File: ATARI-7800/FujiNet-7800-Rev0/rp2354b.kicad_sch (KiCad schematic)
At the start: 46 parts, among them J2 DBG UART, Q1 2N7002, SW1 RESET, SW2 BOOTSEL, U1 RP2354B, Y1 12MHz

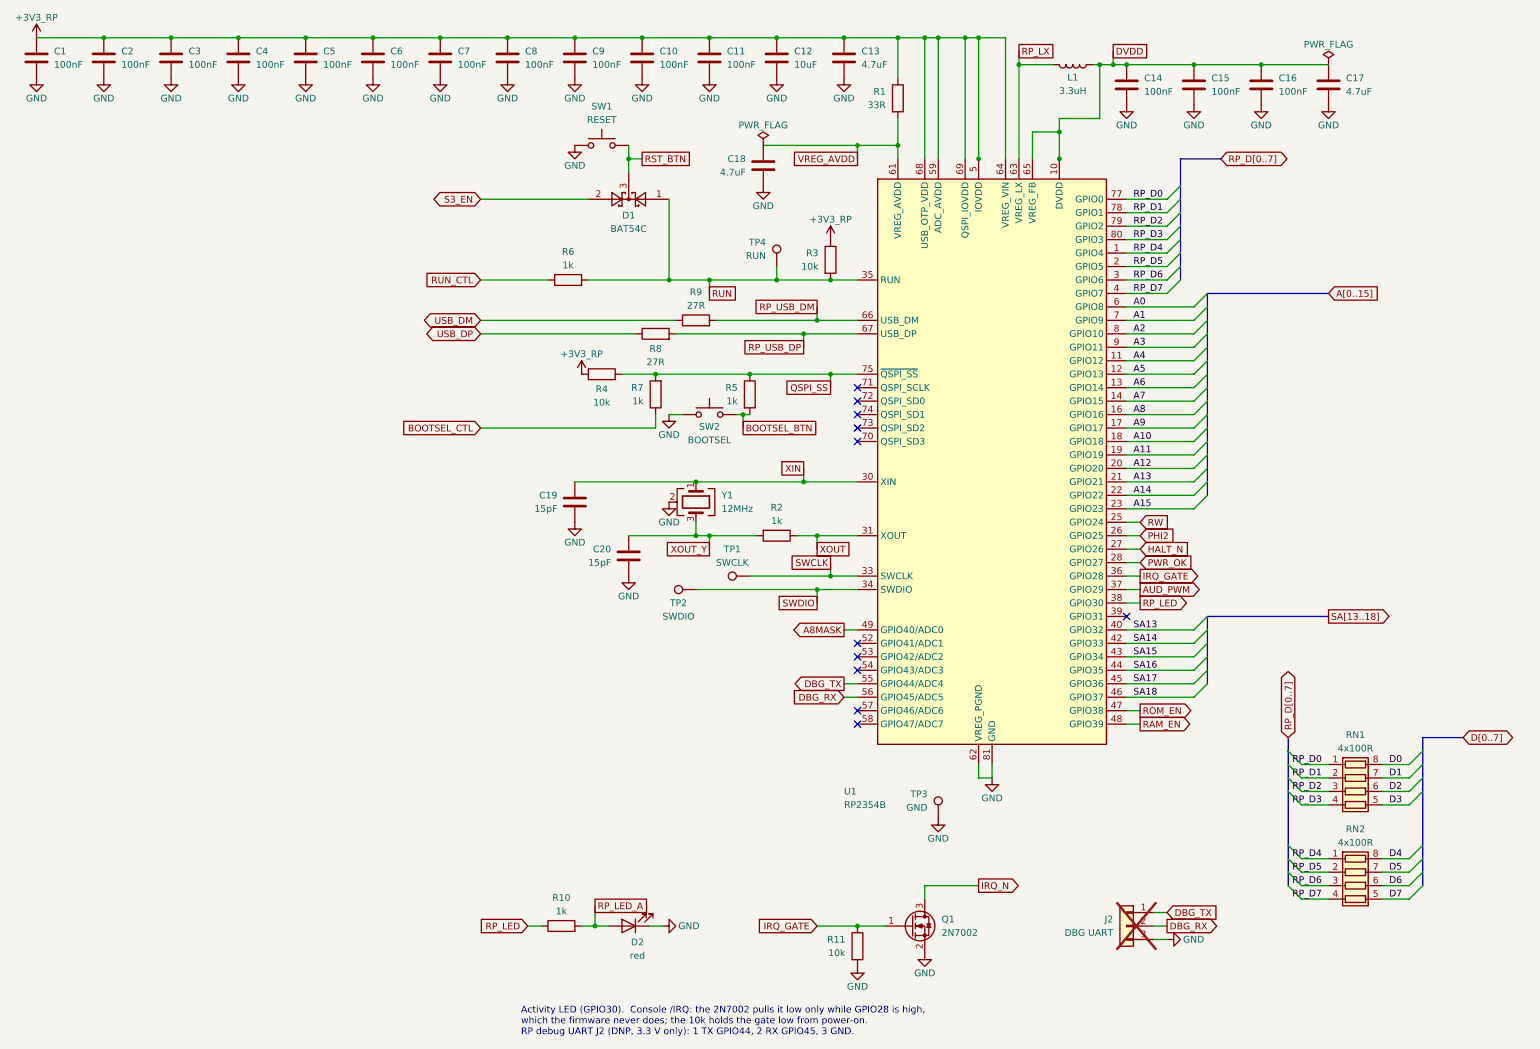
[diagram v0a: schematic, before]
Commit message: ATARI-7800 Rev0: fix the edge, audit the circuit, redraw from the slot, place the board
Edge (board-killer in the schematic-only footprint): the 7800 edge has 18
positions at 2.54 mm with key slots at 3 and 16 for the console's plastic
keys. Pins 1, 2, 15, 16 (and 32, 31, 18, 17) sat one pitch inward, on the
key positions, with no slots and a 42.6 mm tab. tools/edge_geom.py now holds
the geometry (47.0 mm tab, slots centred on +-16.51, 2.4 x 10 mm);
tools/audit/edge_orientation.py checks it against Otaku-flash, tdididit's
boards, the a78-devcart gerbers and this repo's working FujiPlusCart
prototype gerbers (faces and power fingers).

Circuit (console research: Atari C025231 schematic, GCC1702B MARIA spec):
- 4.7k pull-downs on ROM_EN / RAM_EN / A8MASK (RP2350-E9)
- 1k at the /HALT finger (MARIA's HALT is a weak MOS output)
- 10 uF at the console 5V finger; bring-up test pads
- TS-1187A buttons and WS2812C-2020-V1 (the TL3342 and WS2812B-2020
  had 5 in stock at JLC); manufacturer fields for PCBWay
No glue change: R/W is pulled up during MARIA DMA, and the console gates
A15/A14/A12 low while its BIOS is mapped, so CARTSEL never fights it.

Schematic: SMS Rev0's hierarchy (wired root block diagram, hierarchical
labels, netlist parity); sheets in flow order from the slot; the glue
redrawn as a left-to-right gate-depth diagram; references renumbered
from the slot. ERC 0, check_nets 383/383, check_glue 4096/4096.

Board (not yet routed): SMS Rev0's 6-layer pipeline ported. A 72.4 x 115 mm
outline: the stock T-bar width on a 47 x 16.5 mm tab, with the key slots
cut in. Placement variant A (RP over the address fingers, SRAM over the
data fingers): unrouted DRC 0 errors, parity 0, check_vias 0. Shell:
case/FujiNet-7800-Shell.scad. README still describes the old board.

Co-Authored-By: Claude Opus 5.5 <noreply@anthropic.com>
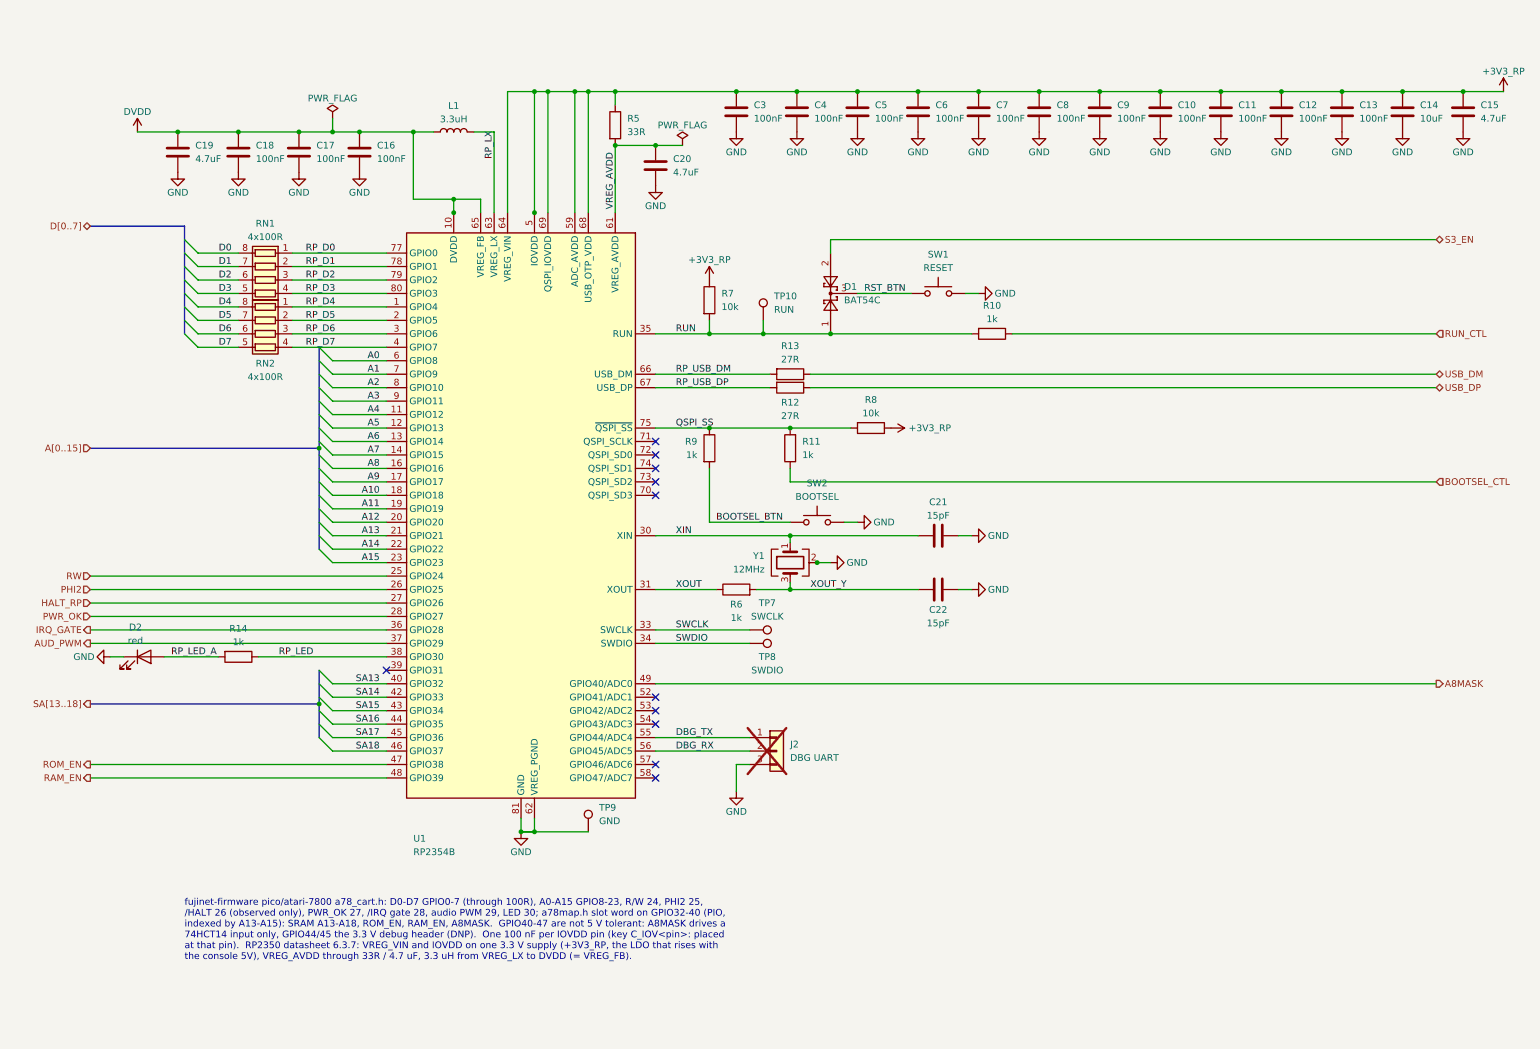
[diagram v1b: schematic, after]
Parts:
- removed C1, C2: 100nF, FujiNet-7800:C_0603_1608Metric, symbol Device:C
- removed Q1: 2N7002, FujiNet-7800:SOT-23, symbol Transistor_FET:2N7002
- removed R1: 33R, FujiNet-7800:R_0603_1608Metric, symbol Device:R
- removed R2: 1k, FujiNet-7800:R_0603_1608Metric, symbol Device:R
- removed R3, R4: 10k, FujiNet-7800:R_0603_1608Metric, symbol Device:R
- removed TP1: SWCLK, FujiNet-7800:TestPoint_Pad_D1.5mm, symbol Connector:TestPoint
- removed TP2: SWDIO, FujiNet-7800:TestPoint_Pad_D1.5mm, symbol Connector:TestPoint
- removed TP3: GND, FujiNet-7800:TestPoint_Pad_D1.5mm, symbol Connector:TestPoint
- removed TP4: RUN, FujiNet-7800:TestPoint_Pad_D1.5mm, symbol Connector:TestPoint
- added C21, C22: 15pF, FujiNet-7800:C_0603_1608Metric, symbol Device:C
- added R12, R13: 27R, FujiNet-7800:R_0603_1608Metric, symbol Device:R
- added R14: 1k, FujiNet-7800:R_0603_1608Metric, symbol Device:R
- added TP10: RUN, FujiNet-7800:TestPoint_Pad_D1.5mm, symbol Connector:TestPoint
- added TP7: SWCLK, FujiNet-7800:TestPoint_Pad_D1.5mm, symbol Connector:TestPoint
- added TP8: SWDIO, FujiNet-7800:TestPoint_Pad_D1.5mm, symbol Connector:TestPoint
- added TP9: GND, FujiNet-7800:TestPoint_Pad_D1.5mm, symbol Connector:TestPoint
- C12: value 10uF -> 100nF; LCSC C19702 -> C14663; MPN CL10A106KP8NNNC -> CC0603KRX7R9BB104
- C13, C17, C18: value 4.7uF -> 100nF; LCSC C19666 -> C14663; MPN CL10A475KO8NNNC -> CC0603KRX7R9BB104
- C14: value 100nF -> 10uF; LCSC C14663 -> C19702; MPN CC0603KRX7R9BB104 -> CL10A106KP8NNNC
- C15: value 100nF -> 4.7uF; LCSC C14663 -> C19666; MPN CC0603KRX7R9BB104 -> CL10A475KO8NNNC
- C19, C20: value 15pF -> 4.7uF; LCSC C1644 -> C19666; MPN CL10C150JB8NNNC -> CL10A475KO8NNNC
- R11: value 10k -> 1k; LCSC C25804 -> C21190; MPN 0603WAF1002T5E -> 0603WAF1001T5E
- R5: value 1k -> 33R; LCSC C21190 -> C23140; MPN 0603WAF1001T5E -> 0603WAF330JT5E
- R7: value 1k -> 10k; LCSC C21190 -> C25804; MPN 0603WAF1001T5E -> 0603WAF1002T5E
- R8: value 27R -> 10k; LCSC C25190 -> C25804; MPN 0603WAF270JT5E -> 0603WAF1002T5E
- R9: value 27R -> 1k; LCSC C25190 -> C21190; MPN 0603WAF270JT5E -> 0603WAF1001T5E
- SW1, SW2: footprint FujiNet-7800:SW_SPST_TL3342 -> FujiNet-7800:SW_SPST_TS-1187A; LCSC C2886898 -> C318884; MPN TL3342F160QG -> TS-1187A-B-A-B
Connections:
- net +3V3_RP: now also C14.1, C15.1, R5.1, R7.1, R8.1
- net BOOTSEL_BTN: now also R9.2; no longer R5.2
- net BOOTSEL_CTL: now also R11.1; no longer R7.1
- net DVDD: now also C18.1, C19.1; no longer C14.1, C15.1
- net GND: now also C21.2, C22.2, TP9.1; no longer R11.2
- net IRQ_GATE: no longer R11.1
- net QSPI_SS: now also R11.2, R8.2, R9.1; no longer R5.1, R7.2
- net RP_LED: now also R14.1; no longer R10.1
- net RP_LED_A: now also R14.2; no longer R10.2
- net RP_USB_DM: now also R13.2; no longer R9.2
- net RP_USB_DP: now also R12.2; no longer R8.2
- net RUN: now also R10.2, R7.2, TP10.1; no longer R6.2
- net RUN_CTL: now also R10.1; no longer R6.1
- net SWCLK: now also TP7.1
- net SWDIO: now also TP8.1
- net USB_DM: now also R13.1; no longer R9.1
- net USB_DP: now also R12.1; no longer R8.1
- net VREG_AVDD: now also C20.1, R5.2; no longer C18.1
- net XIN: now also C21.1; no longer C19.1
- net XOUT: now also R6.1
- net XOUT_Y: now also R6.2, C22.1; no longer C20.1
- net HALT_N renamed HALT_RP
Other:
- note added: "fujinet-firmware pico/atari-7800 a78_cart.h: D0-D7 GPIO0-7 (through 100R), A0-A15 GPIO8-23, R/W 24, PHI2 25, /HALT 26 (observed only), PWR_OK 27, /IRQ gate 28, audio PWM 29, LED 30; a78map.h slot word on GPIO32-40 (PIO, indexed by A13-A15): SRAM A13-A18, ROM_EN, RAM_EN, A8MASK. GPIO40-47 are not 5 V tolerant: A8MASK drives a 74HCT14 input only, GPIO44/45 the 3.3 V debug header (DNP). One 100 nF p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"
- note removed: "Activity LED (GPIO30). Console /IRQ: the 2N7002 pulls it low only while GPIO28 is high, which the firmware never does; the 10k holds the gate low from power-on. RP debug UART J2 (DNP, 3.3 V only): 1 TX GPIO44, 2 RX GPIO45, 3 GND."
- title: FujiNet 7800 Rev0 - RP2354B bus controller -> FujiNet 7800 Rev0 - RP2354B bus controller, slot table
- moved on the sheet: C10, C11, C12, C13, C14, C15, C16, C17, C18, C19, C20, C3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
